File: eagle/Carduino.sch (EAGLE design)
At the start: 77 parts, among them IC1 DS3231M+TRL, IC2 FT232RL, IC3 SN74HCS596DR, IC4 SN74HCS596DR, IC5 SN74HCS596DR, IC6 SN74HCS596DR, IC8 ATTINY404-SSNR, U1 BAT-HLD-012-SMT

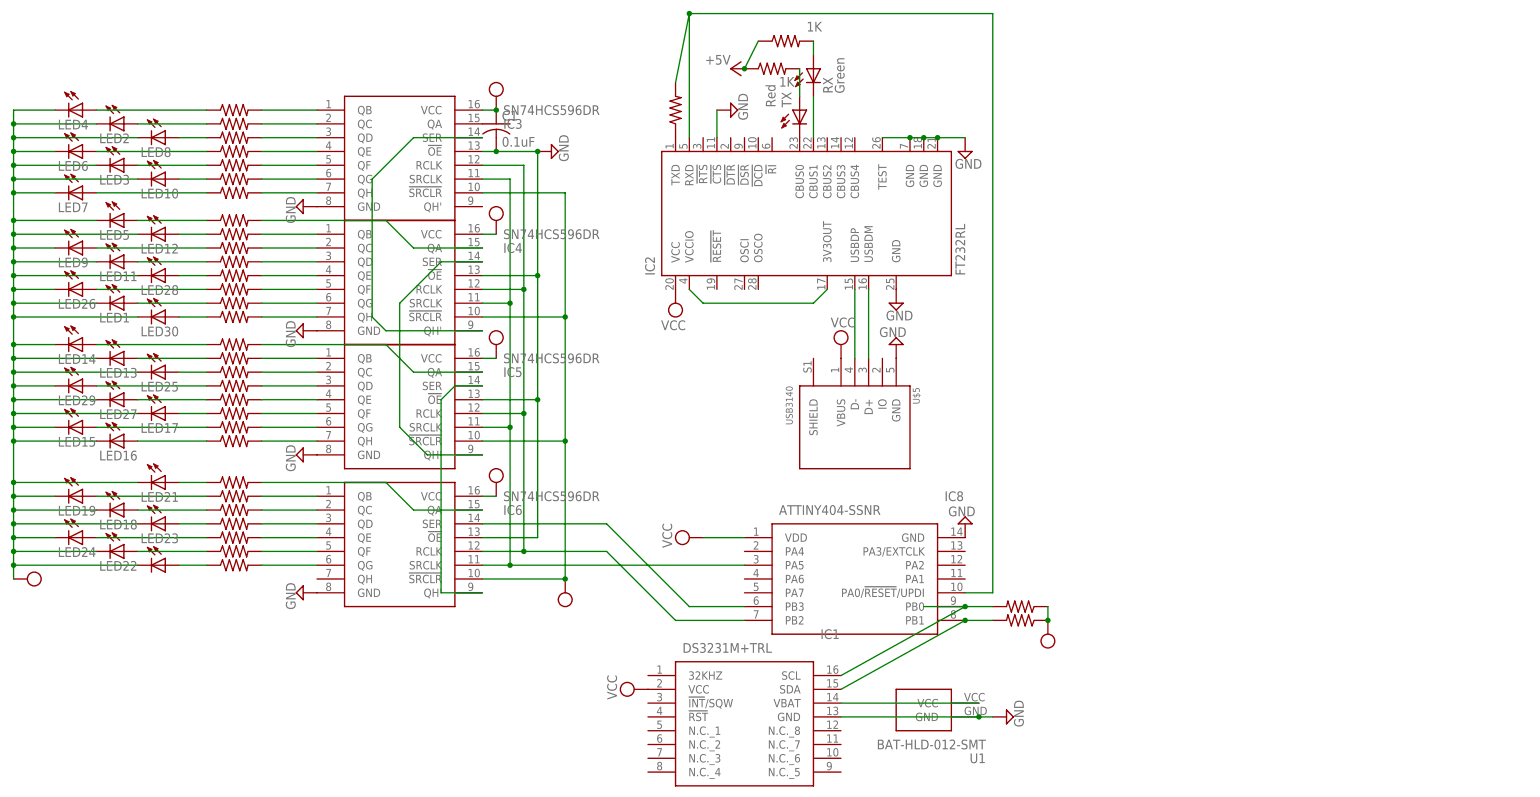
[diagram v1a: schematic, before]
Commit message: added realtime clock
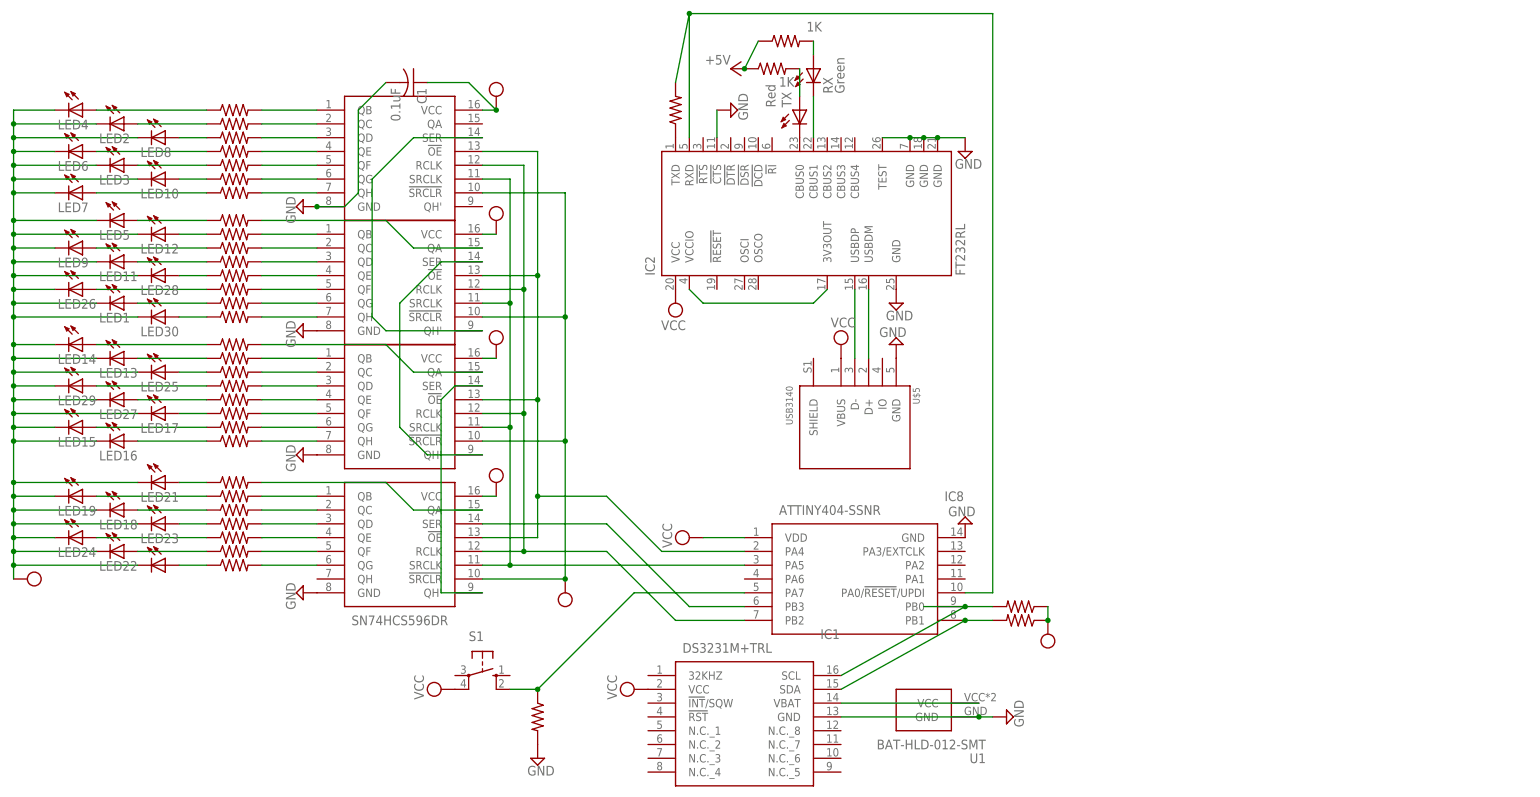
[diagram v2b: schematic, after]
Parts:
- added R6: 4.7K, adafruit:R-US_R0805
- added S1: (no value), adafruit:40-XX-ROUND
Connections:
- new net N$34: IC8.PA7, R6.1, S1.S1
- new net N$35: IC3.!OE, IC4.!OE, IC5.!OE, IC6.!OE, IC8.PA4
- net GND: now also R6.2; no longer IC3.!OE, IC4.!OE, IC5.!OE, IC6.!OE
- net VCC: now also S1.P1
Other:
- moved on the sheet: C1

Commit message: better use of button to adjust dots
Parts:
- added C2: 4.7uF, resistor:C-USC1206
- added C3: 1uF, resistor:C-USC1206
- added CHARGING: Red, adafruit:LEDCHIP-LED0805
- added CN1: (no value), adafruit:JST_2PIN-SMT-RA
- added IC7: NTMD4184PFR2G, SamacSys_Parts:NTMD4184PFR2G
- added IC9: MCP73831T-3ACI_OT, SamacSys_Parts:MCP73831T-3ACI_OT
- added R16: 470, adafruit:R-US_R0805
- added R21: 100K, adafruit:R-US_R0805
- added R22: 10K, adafruit:R-US_R0805
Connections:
- removed net +5V: R2.1, R3.1
- new net N$36: IC7.A_1, IC7.G, R21.1
- new net N$37: IC9.PROG, R22.1
- new net N$38: C2.1, CN1.2, IC7.D_1, IC9.VBAT
- new net N$39: CHARGING.C, IC9.STAT
- new net N$40: CHARGING.A, R16.1
- net GND: now also C2.2, C3.1, CN1.1, IC9.VSS, R21.2, R22.2
- net VCC: now also C3.2, IC7.C_2, IC7.S, IC9.VDD, R16.2, R2.1, R3.1

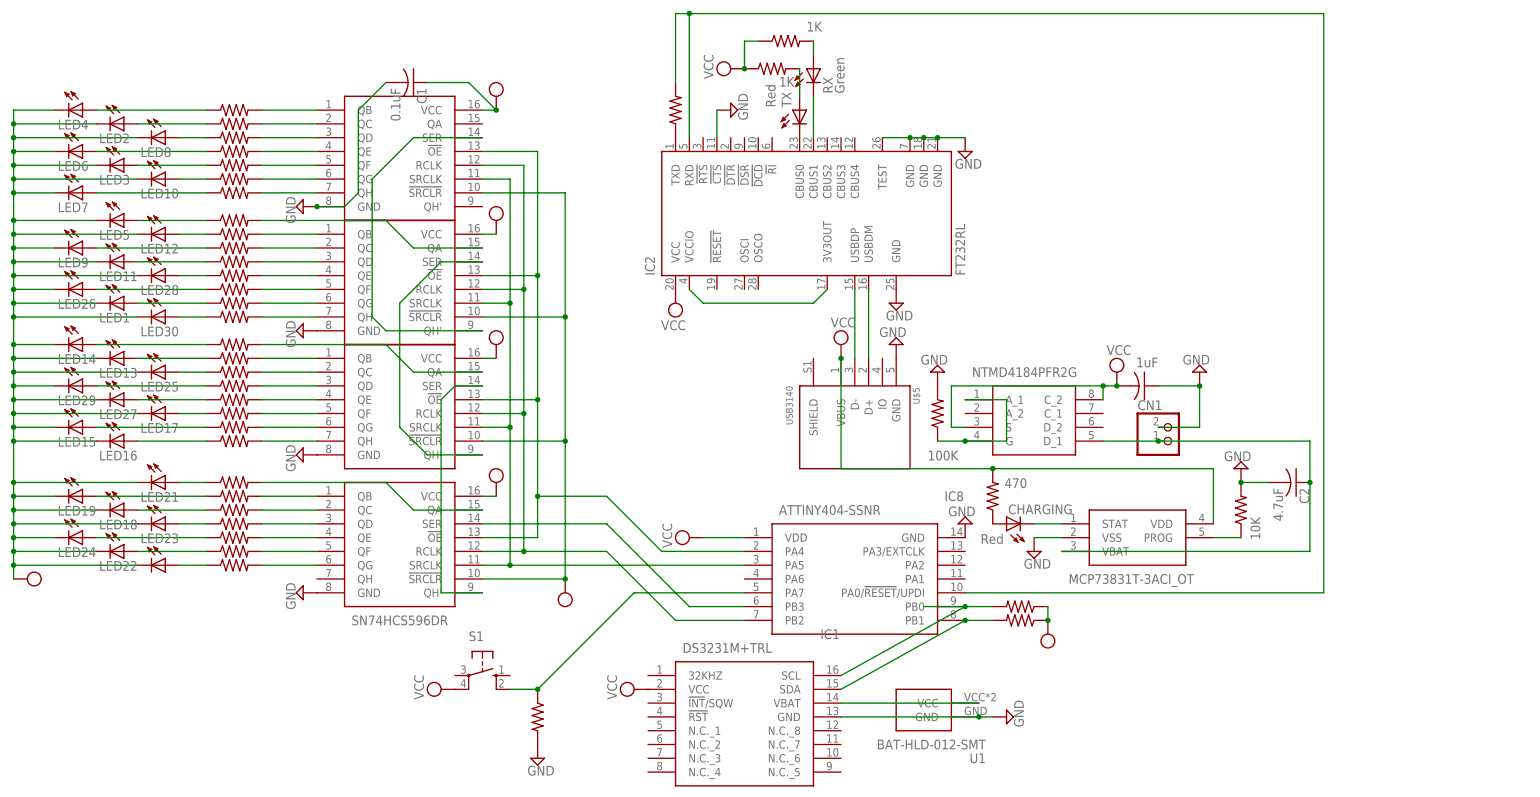
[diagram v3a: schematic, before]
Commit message: new clock and ftdi chips
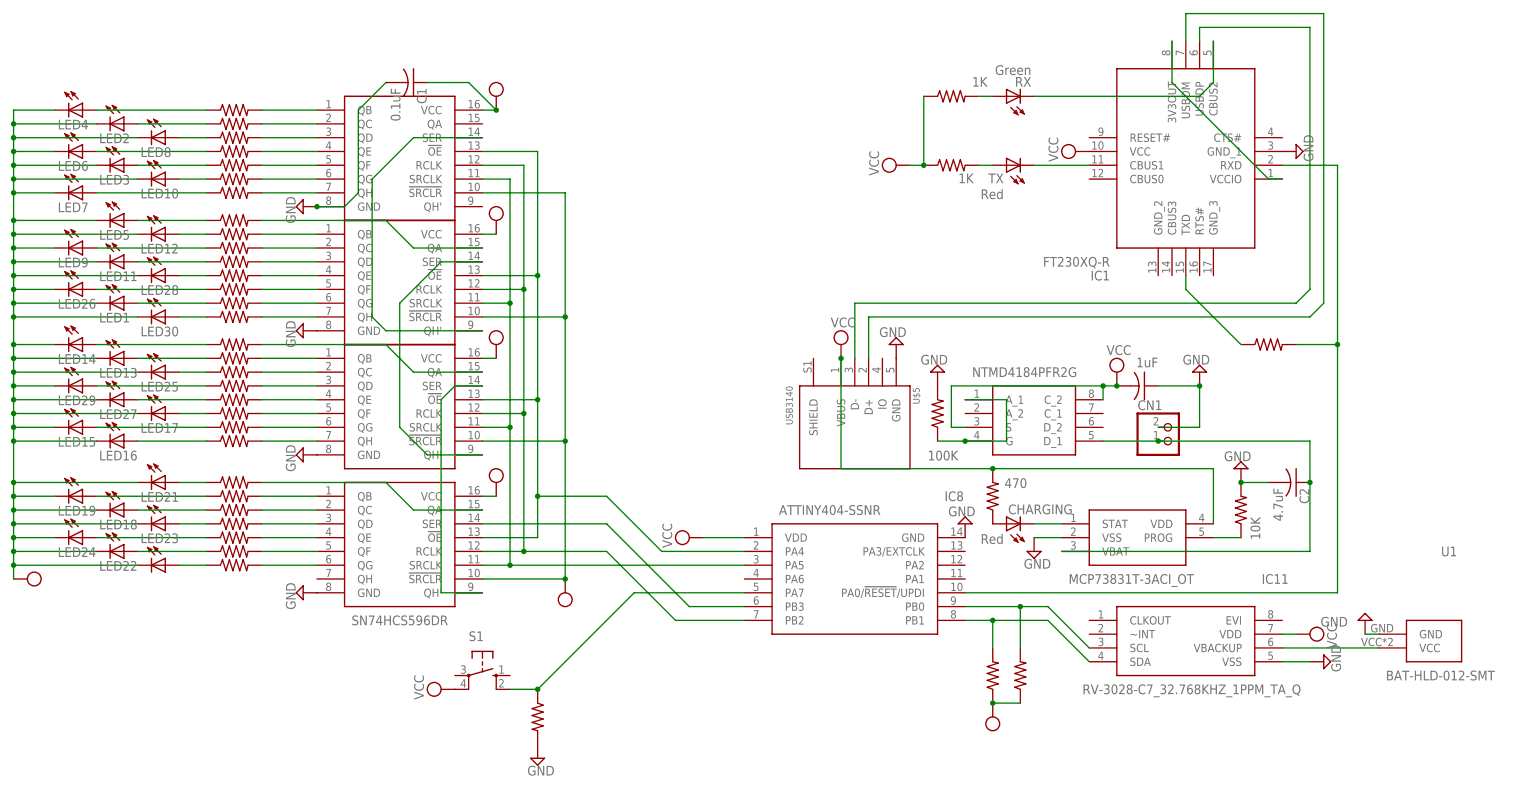
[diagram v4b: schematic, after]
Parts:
- removed IC2: FT232RL, ftdichip:FT232RL
- removed R1: 470, adafruit:R-US_R0805
- added IC11: RV-3028-C7_32.768KHZ_1PPM_TA_Q, SamacSys_Parts:RV-3028-C7_32.768KHZ_1PPM_TA_Q
- added R23: 470, adafruit:R-US_R0805
- IC1: value DS3231M+TRL -> FT230XQ-R; device SamacSys_Parts:DS3231M+TRL -> SamacSys_Parts:FT230XQ-R
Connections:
- removed net N$101: IC2.3V3OUT, IC2.VCCIO
- removed net N$102: IC2.TXD, R1.1
- removed net N$107: IC2.CBUS1, RX.C
- new net N$41: IC1.TXD, R23.1
- new net N$42: IC1.3V3OUT, IC1.VCCIO
- new net N$43: IC1.CBUS1, TX.C
- net GND: now also IC1.GND_1, IC11.VSS; no longer IC1.GND, IC2.!CTS, IC2.GND, IC2.GND@1, IC2.GND@2, IC2.GND@A, IC2.TEST
- net N$100: now also IC1.USBDP; no longer IC2.USBDP
- net N$103: now also IC1.RXD, R23.2; no longer IC2.RXD, R1.2
- net N$106: now also IC1.CBUS2, RX.C; no longer IC2.CBUS0, TX.C
- net N$31: now also IC11.SDA; no longer IC1.SDA
- net N$32: now also IC11.SCL; no longer IC1.SCL
- net N$33: now also IC11.VBACKUP; no longer IC1.VBAT
- net N$99: now also IC1.USBDM; no longer IC2.USBDM
- net VCC: now also IC11.VDD; no longer IC2.VCC
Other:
- moved on the sheet: RX, TX, U1
